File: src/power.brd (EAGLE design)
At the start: 36 x 88.5 mm, 61 parts, among them CON1 PINHEAD_2X02-0877590414, CON2 PINHEAD_2X02-0877590414, CON3 PINHEAD_2X02-0877590414, CON4 PINHEAD_2X02-0877590414, CON5 PINHEAD_2X02-0877590414, CON6 PINHEAD_2X04-SMD-2-MALE, CON7 PINHEAD_2X02-0877590414, IC1 UCC27282-SOIC8, IC2 UCC27282-SOIC8, IC3 UCC27282-SOIC8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

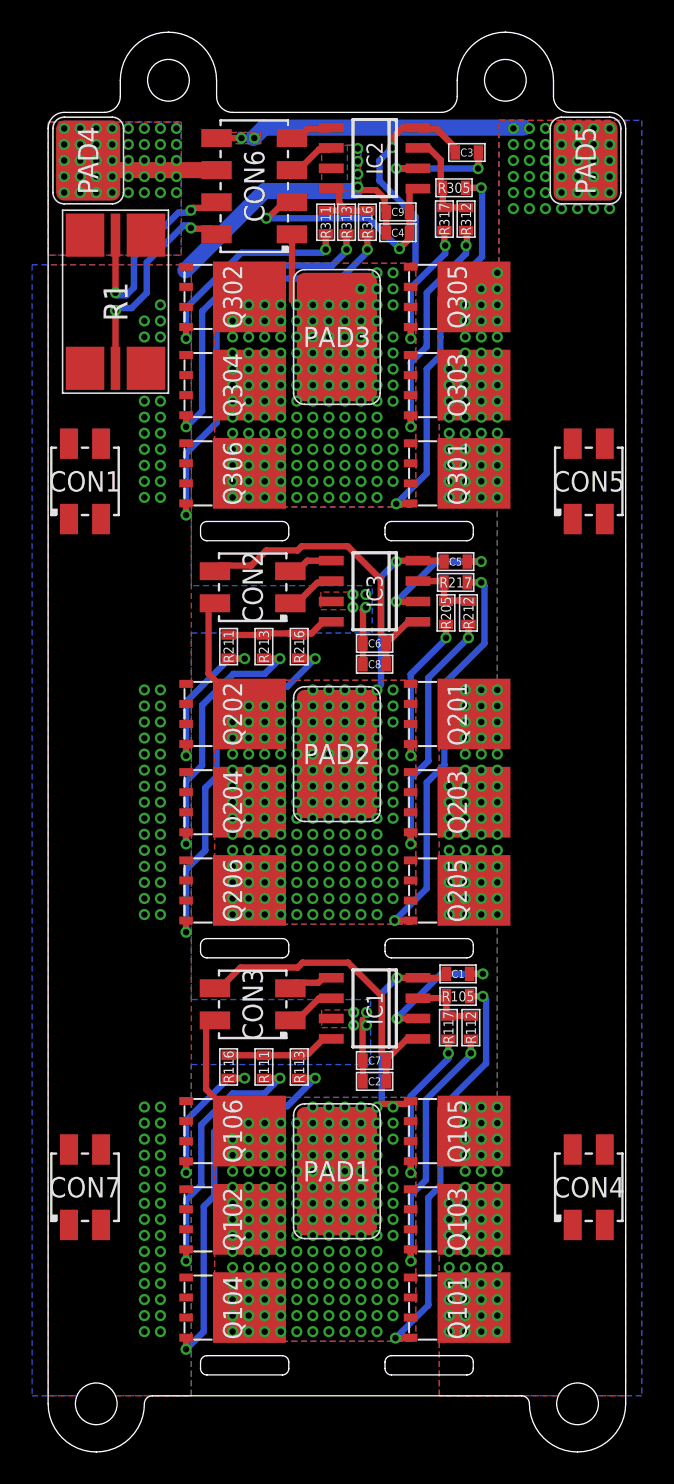
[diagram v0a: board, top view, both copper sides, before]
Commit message: Power PCB update
DRC  errors resolvinnng
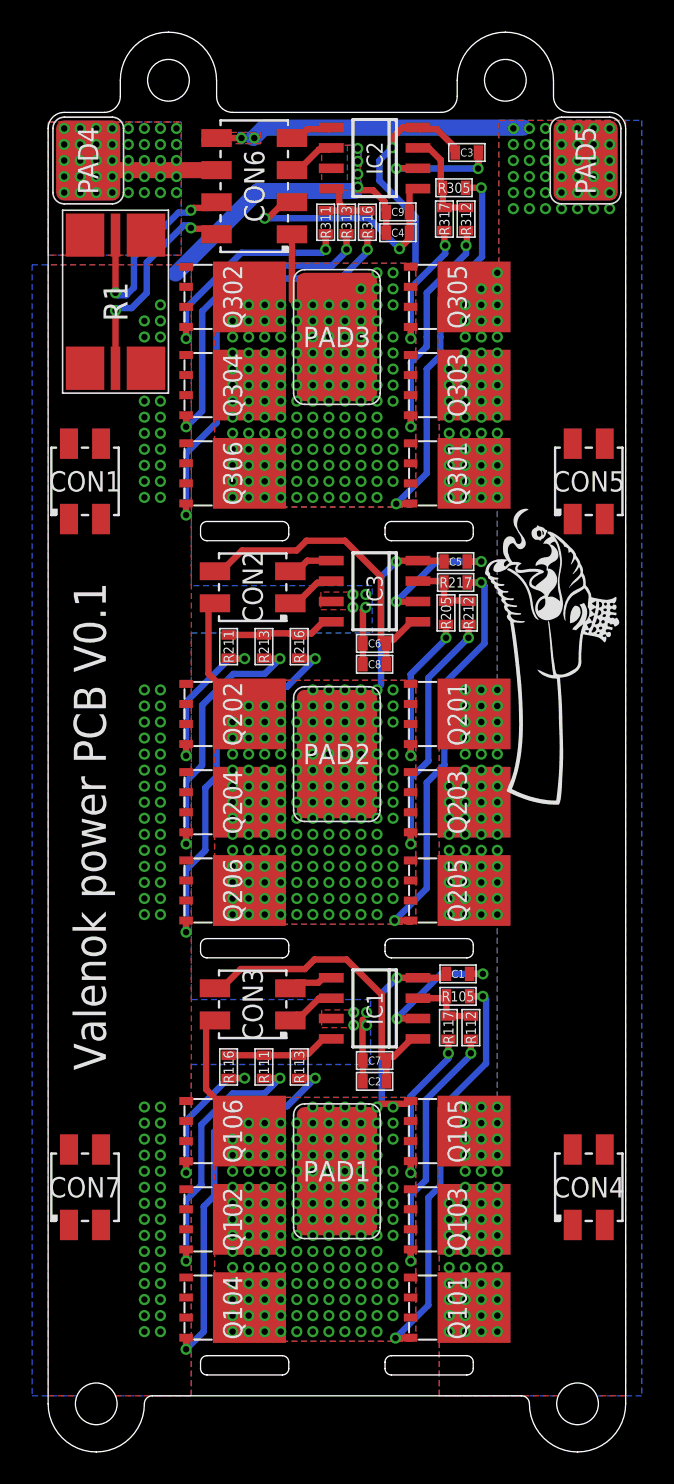
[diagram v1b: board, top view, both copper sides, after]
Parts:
- added U$1: (no value), logo:DRAGON-18X7
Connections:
- removed net VDD_15V: C2.1, C4.1, C6.1, C7.1, C8.1, C9.1, CON2.4, CON3.4, CON6.3, IC1.1, IC2.1, IC3.1
- new net 97: C2.1, C7.1, CON3.4, IC1.1
- new net N$3: C4.1, C9.1, CON6.3, IC2.1
- new net N$4: C6.1, C8.1, CON2.4, IC3.1
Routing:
- net VDD_15V: track 55.7 -> 0.00 mm, vias 2 -> 0
- net N$4: track 0.00 -> 20.3 mm
- net 97: track 0.00 -> 20.2 mm
- net N$3: track 0.00 -> 15.8 mm, vias 0 -> 2
- net PGND: track 24.6 -> 25.1 mm
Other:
- board text added: "Valenok power PCB V0.1"
